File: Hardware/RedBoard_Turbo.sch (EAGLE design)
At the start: 61 parts, among them Q1 2.5A/30V, Q2 2N7002PW, U1 MCP73831, U2 74AHC1G125, U3 3.3V, U4 ATSAMD21G-A, U5 W25Q32FV, Y1 32.768kHz

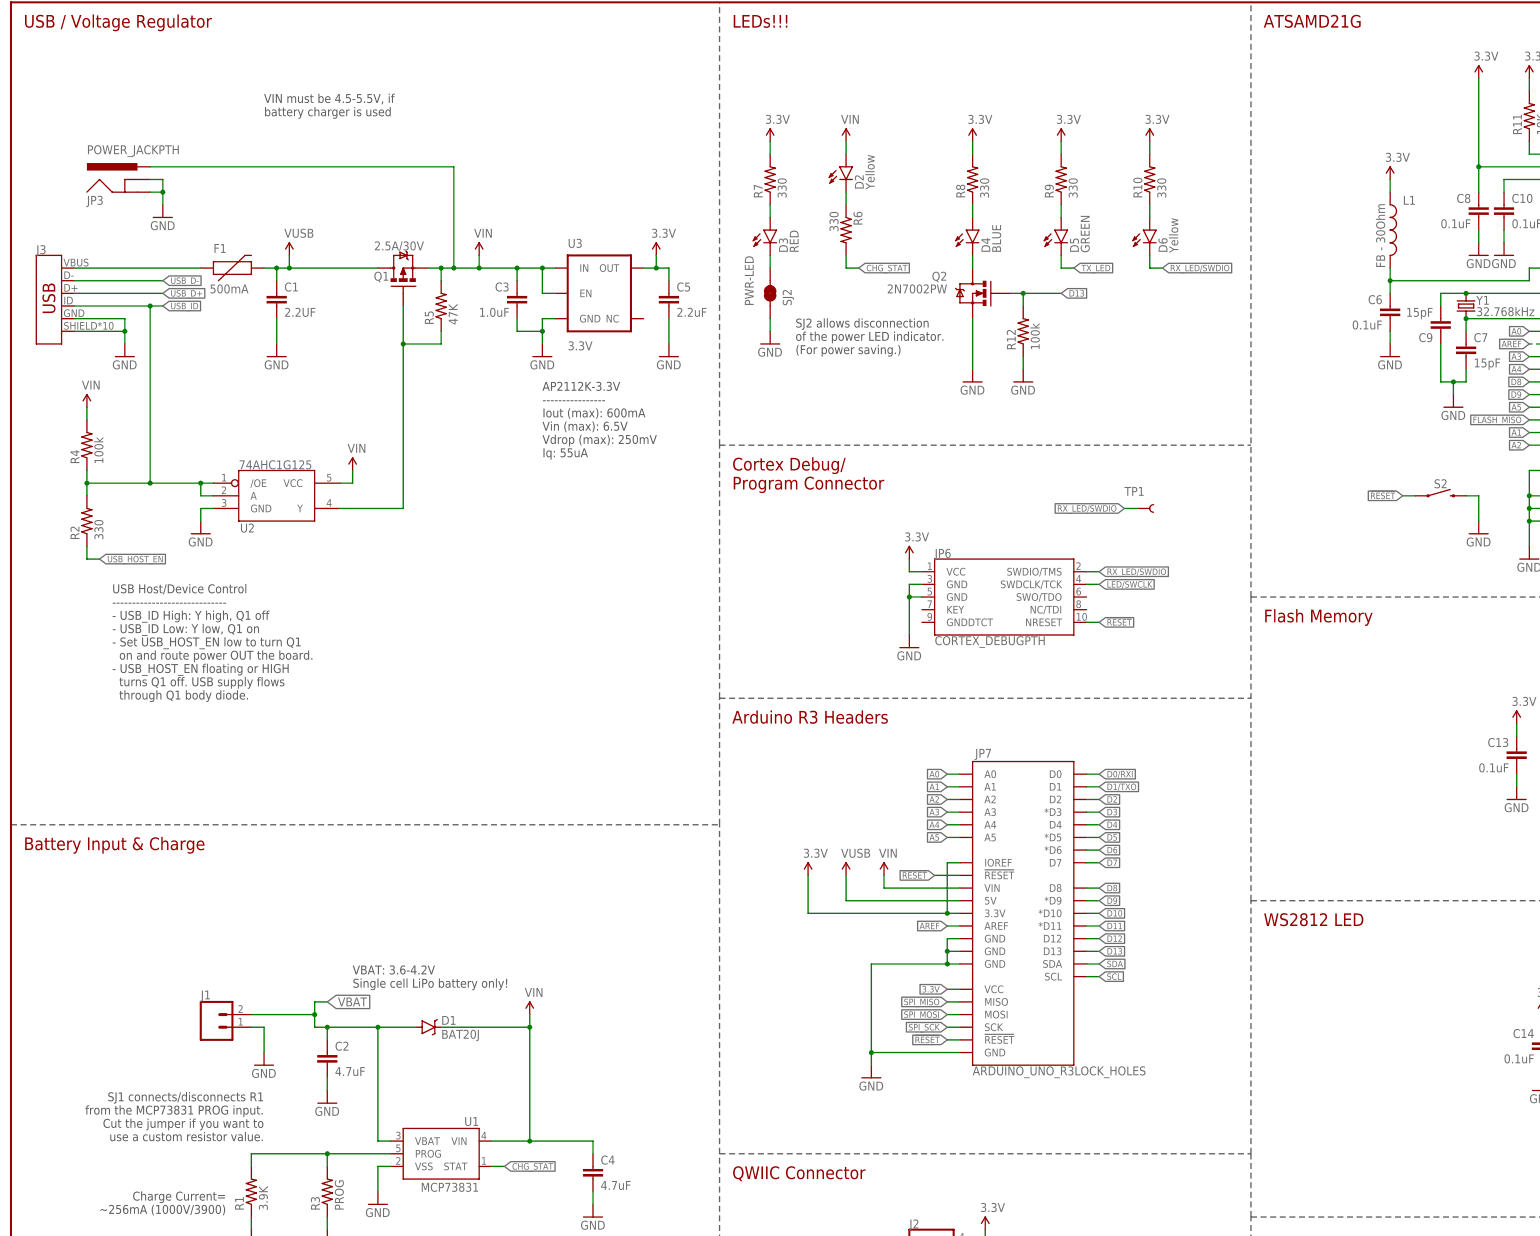
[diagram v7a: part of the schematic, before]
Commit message: Updated schematic
Updated part names and removed extra text
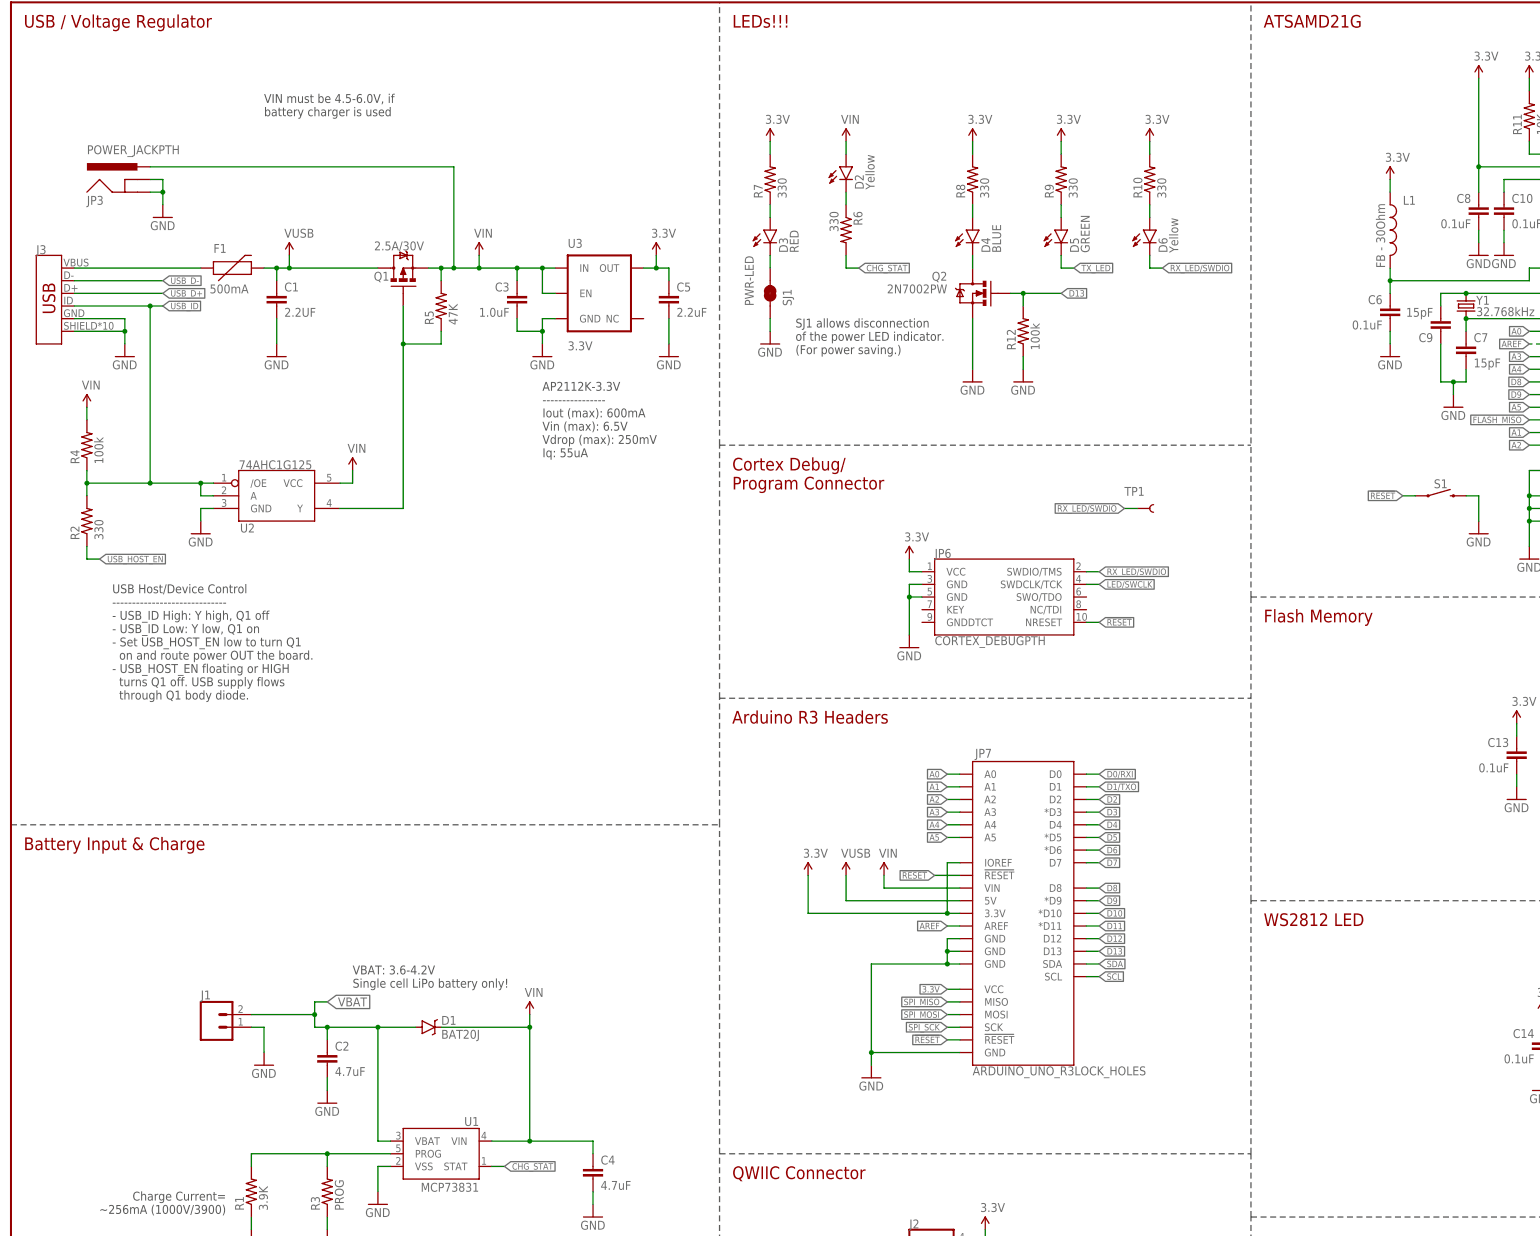
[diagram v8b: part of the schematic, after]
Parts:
- renumbered S2 to S1, SJ2 to SJ1
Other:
- note added: "SJ1 allows disconnection of the power LED indicator. (For power saving.)"
- note added: "VIN must be 4.5-6.0V, if battery charger is used"
- note removed: "SJ1 connects/disconnects R1 from the MCP73831 PROG input. Cut the jumper if you want to use a custom resistor value."
- note removed: "SJ2 allows disconnection of the power LED indicator. (For power saving.)"
- note removed: "VIN must be 4.5-5.5V, if battery charger is used"
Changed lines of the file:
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@@
 <part name="LOGO3" library="SparkFun-Aesthetics" deviceset="OSHW-LOGO" device="S"/>
 <part name="LOGO1" library="SparkFun-Aesthetics" deviceset="SFE_LOGO_NAME_FLAME" device=".2_INCH" value="SFE_LOGO_NAME_FLAME.2_INCH"/>
-<part name="SJ2" library="SparkFun-Passives" deviceset="JUMPER-PAD-2-NC_BY_TRACE" device="NO_SILK" value="PWR-LED"/>
+<part name="SJ1" library="SparkFun-Passives" deviceset="JUMPER-PAD-2-NC_BY_TRACE" device="NO_SILK" value="PWR-LED"/>
 <part name="FID2" library="SparkFun-Aesthetics" deviceset="FIDUCIAL" device="1X2"/>
 <part name="FID1" library="SparkFun-Aesthetics" deviceset="FIDUCIAL" device="1X2"/>
@@
 <part name="FID4" library="SparkFun-Aesthetics" deviceset="FIDUCIAL" device="1X2"/>
 <part name="TP1" library="SparkFun-Connectors" deviceset="TEST-POINT" device="TP_15TH_THRU"/>
-<part name="S2" library="SparkFun-Switches" deviceset="MOMENTARY-SWITCH-SPST" device="-SMD-5.2-TALL-REDUNDANT" value=""/>
+<part name="S1" library="SparkFun-Switches" deviceset="MOMENTARY-SWITCH-SPST" device="-SMD-5.2-TALL-REDUNDANT" value=""/>
 </parts>
 <sheets>
@@
 <text x="43.18" y="40.64" size="1.778" layer="97" rot="R180">Charge Current=
 ~256mA (1000V/3900)</text>
-<text x="50.8" y="50.8" size="1.778" layer="97" align="bottom-right">SJ1 connects/disconnects R1
-from the MCP73831 PROG input.
-Cut the jumper if you want to
-use a custom resistor value.</text>
 <wire x1="248.92" y1="35.56" x2="248.92" y2="48.26" width="0.2032" layer="97" style="longdash"/>
 <wire x1="248.92" y1="48.26" x2="248.92" y2="99.06" width="0.2032" layer="97" style="longdash"/>
@@
 <wire x1="0" y1="114.3" x2="142.24" y2="114.3" width="0.2032" layer="97" style="longdash"/>
 <text x="2.54" y="111.76" size="2.54" layer="94" align="top-left">Battery Input &amp; Charge</text>
-<text x="157.48" y="215.9" size="1.778" layer="97" align="top-left">SJ2 allows disconnection
+<text x="157.48" y="215.9" size="1.778" layer="97" align="top-left">SJ1 allows disconnection
 of the power LED indicator.
 (For power saving.)</text>
@@
 <wire x1="248.92" y1="160.02" x2="431.8" y2="160.02" width="0.2032" layer="97" style="longdash"/>
 <wire x1="248.92" y1="35.56" x2="330.2" y2="35.56" width="0.2032" layer="97" style="longdash"/>
-<text x="50.8" y="256.54" size="1.778" layer="97">VIN must be 4.5-5.5V, if
+<text x="50.8" y="256.54" size="1.778" layer="97">VIN must be 4.5-6.0V, if
 battery charger is used</text>
 <text x="314.96" y="256.54" size="1.778" layer="97">ATSAMD21G18
@@
 <instance part="LOGO3" gate="G$1" x="317.5" y="10.16" smashed="yes"/>
 <instance part="LOGO1" gate="G$1" x="251.46" y="5.08" smashed="yes"/>
-<instance part="SJ2" gate="G$1" x="152.4" y="220.98" smashed="yes" rot="MR90">
+<instance part="SJ1" gate="G$1" x="152.4" y="220.98" smashed="yes" rot="MR90">
 <attribute name="NAME" x="154.94" y="218.44" size="1.778" layer="95" rot="MR90"/>
 <attribute name="VALUE" x="147.32" y="218.44" size="1.778" layer="96" rot="MR90"/>
@@
 <attribute name="NAME" x="223.52" y="180.34" size="1.778" layer="95" font="vector"/>
 </instance>
-<instance part="S2" gate="G$1" x="287.02" y="180.34"/>
+<instance part="S1" gate="G$1" x="287.02" y="180.34"/>
 </instances>
 <busses>
@@
 <segment>
 <pinref part="GND14" gate="1" pin="GND"/>
-<pinref part="SJ2" gate="G$1" pin="1"/>
+<pinref part="SJ1" gate="G$1" pin="1"/>
 <wire x1="152.4" y1="215.9" x2="152.4" y2="213.36" width="0.1524" layer="91"/>
 </segment>
@@
 <wire x1="294.64" y1="175.26" x2="294.64" y2="180.34" width="0.1524" layer="91"/>
 <wire x1="294.64" y1="180.34" x2="292.1" y2="180.34" width="0.1524" layer="91"/>
-<pinref part="S2" gate="G$1" pin="2"/>
+<pinref part="S1" gate="G$1" pin="2"/>
 </segment>
 <segment>
@@
 <wire x1="281.94" y1="180.34" x2="279.4" y2="180.34" width="0.1524" layer="91"/>
 <label x="279.4" y="180.34" size="1.27" layer="95" rot="R180" xref="yes"/>
-<pinref part="S2" gate="G$1" pin="1"/>
+<pinref part="S1" gate="G$1" pin="1"/>
 </segment>
 </net>
@@
 <segment>
 <pinref part="D3" gate="G$1" pin="C"/>
-<pinref part="SJ2" gate="G$1" pin="2"/>
+<pinref part="SJ1" gate="G$1" pin="2"/>
 <wire x1="152.4" y1="226.06" x2="152.4" y2="228.6" width="0.1524" layer="91"/>
 </segment>
